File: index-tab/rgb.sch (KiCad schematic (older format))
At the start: 0 parts

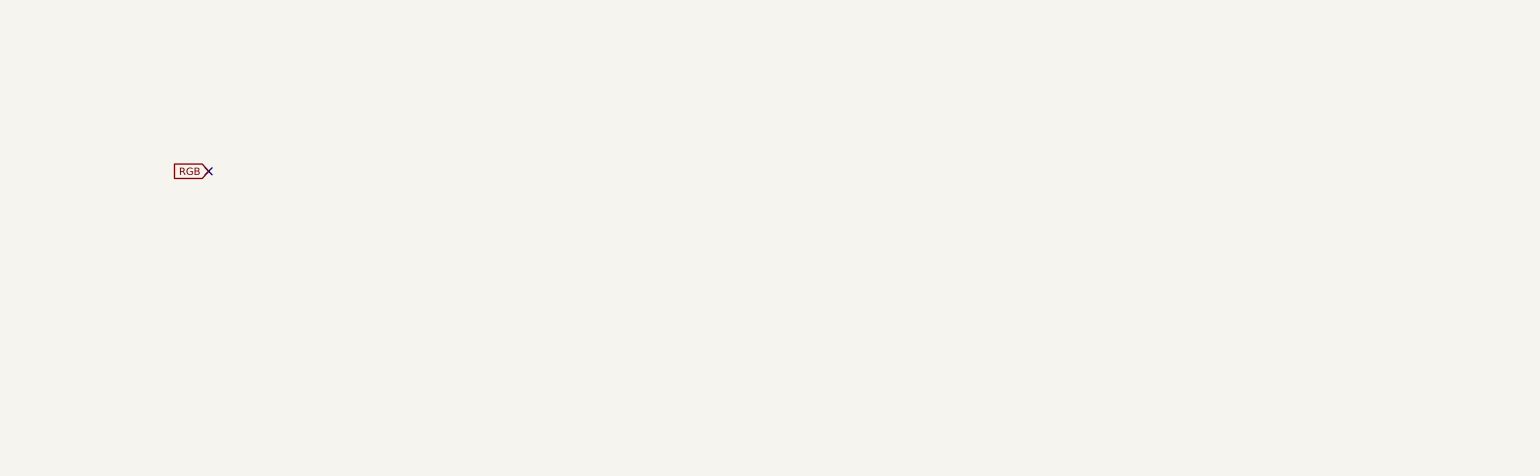
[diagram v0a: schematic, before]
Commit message: added backlight and rgb
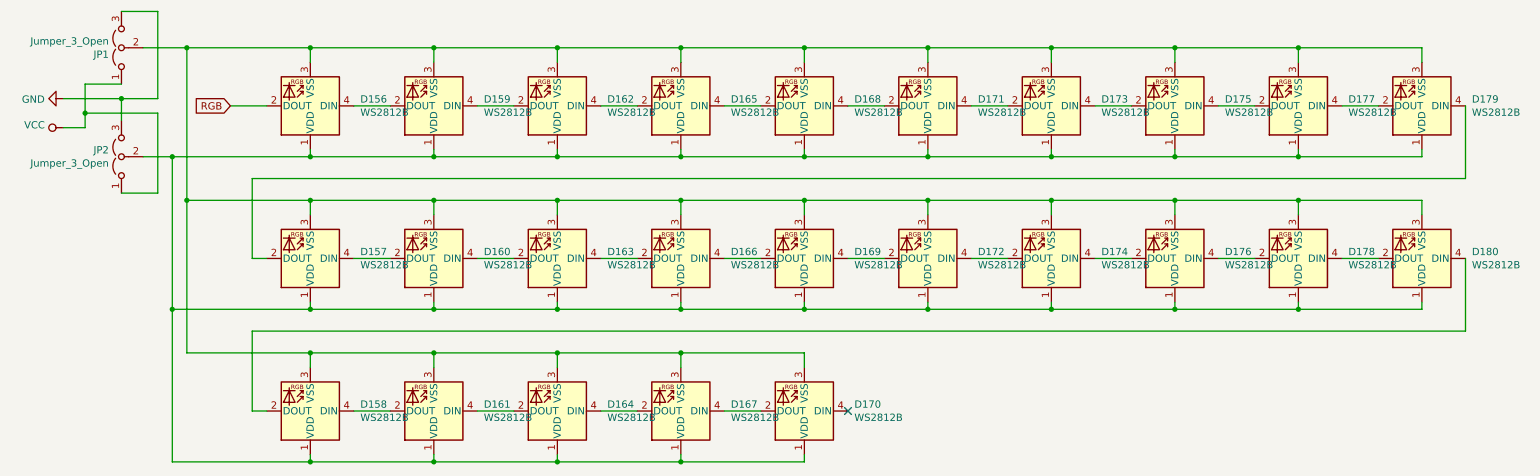
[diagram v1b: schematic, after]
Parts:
- added D156, D157, D158, D159, D160, D161, D162, D163, D164, D165, D166, D167, D168, D169, D170, D171, D172, D173, D174, D175, D176, D177, D178, D179, D180: WS2812B, LED_SMD:LED_WS2812B_PLCC4_5.0x5.0mm_P3.2mm, symbol LED:WS2812B
- added JP1, JP2: Jumper_3_Open, symbol Jumper:Jumper_3_Open
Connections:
- net RGB: now also D156.2 (DOUT)
- new net: D156.3 (VSS), D157.3 (VSS), D158.3 (VSS), D159.3 (VSS), D160.3 (VSS), D161.3 (VSS), D162.3 (VSS), D163.3 (VSS), D164.3 (VSS), D165.3 (VSS), D166.3 (VSS), D167.3 (VSS), D168.3 (VSS), D169.3 (VSS), D170.3 (VSS), D171.3 (VSS), D172.3 (VSS), D173.3 (VSS), D174.3 (VSS), D175.3 (VSS), D176.3 (VSS), D177.3 (VSS), D178.3 (VSS), D179.3 (VSS), D180.3 (VSS), JP1.2 (C)
- new net: D156.1 (VDD), D157.1 (VDD), D158.1 (VDD), D159.1 (VDD), D160.1 (VDD), D161.1 (VDD), D162.1 (VDD), D163.1 (VDD), D164.1 (VDD), D165.1 (VDD), D166.1 (VDD), D167.1 (VDD), D168.1 (VDD), D169.1 (VDD), D170.1 (VDD), D171.1 (VDD), D172.1 (VDD), D173.1 (VDD), D174.1 (VDD), D175.1 (VDD), D176.1 (VDD), D177.1 (VDD), D178.1 (VDD), D179.1 (VDD), D180.1 (VDD), JP2.2 (C)
- new net: D156.4 (DIN), D159.2 (DOUT)
- new net: D159.4 (DIN), D162.2 (DOUT)
- new net: D162.4 (DIN), D165.2 (DOUT)
- new net: D165.4 (DIN), D168.2 (DOUT)
- new net: D168.4 (DIN), D171.2 (DOUT)
- new net: D171.4 (DIN), D173.2 (DOUT)
- new net: D173.4 (DIN), D175.2 (DOUT)
- new net: D175.4 (DIN), D177.2 (DOUT)
- new net: D177.4 (DIN), D179.2 (DOUT)
- new net: D157.2 (DOUT), D179.4 (DIN)
- new net: D157.4 (DIN), D160.2 (DOUT)
- new net: D160.4 (DIN), D163.2 (DOUT)
- new net: D163.4 (DIN), D166.2 (DOUT)
- new net: D166.4 (DIN), D169.2 (DOUT)
- new net: D169.4 (DIN), D172.2 (DOUT)
- new net: D172.4 (DIN), D174.2 (DOUT)
- new net: D174.4 (DIN), D176.2 (DOUT)
- new net: D176.4 (DIN), D178.2 (DOUT)
- new net: D178.4 (DIN), D180.2 (DOUT)
- new net: D158.2 (DOUT), D180.4 (DIN)
- new net: D158.4 (DIN), D161.2 (DOUT)
- new net: D161.4 (DIN), D164.2 (DOUT)
- new net: D164.4 (DIN), D167.2 (DOUT)
- new net: D167.4 (DIN), D170.2 (DOUT)
- new net GND: JP1.3 (B), JP2.3 (B)
- new net VCC: JP1.1 (A), JP2.1 (A)

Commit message: Added footprints to all components, and done some formatting
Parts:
- JP1, JP2: footprint (none) -> Jumper:SolderJumper-3_P1.3mm_Open_Pad1.0x1.5mm
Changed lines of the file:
@@
 F 0 "JP1" V 1304 1387 50  0000 L CNN
 F 1 "Jumper_3_Open" V 1395 1387 50  0000 L CNN
-F 2 "" H 1350 1300 50  0001 C CNN
+F 2 "Jumper:SolderJumper-3_P1.3mm_Open_Pad1.0x1.5mm" H 1350 1300 50  0001 C CNN
 F 3 "~" H 1350 1300 50  0001 C CNN
 	1    1350 1300
@@
 F 0 "JP2" V 1396 2137 50  0000 L CNN
 F 1 "Jumper_3_Open" V 1305 2137 50  0000 L CNN
-F 2 "" H 1350 2050 50  0001 C CNN
+F 2 "Jumper:SolderJumper-3_P1.3mm_Open_Pad1.0x1.5mm" H 1350 2050 50  0001 C CNN
 F 3 "~" H 1350 2050 50  0001 C CNN
 	1    1350 2050
